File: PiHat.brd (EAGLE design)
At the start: 53.7 x 27.8 mm, 13 parts, among them J1 DESTINYSENSORFINAL_SPARKFUN-C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, X2 SCREENBREAKOUT_SCREENBREAKOUT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

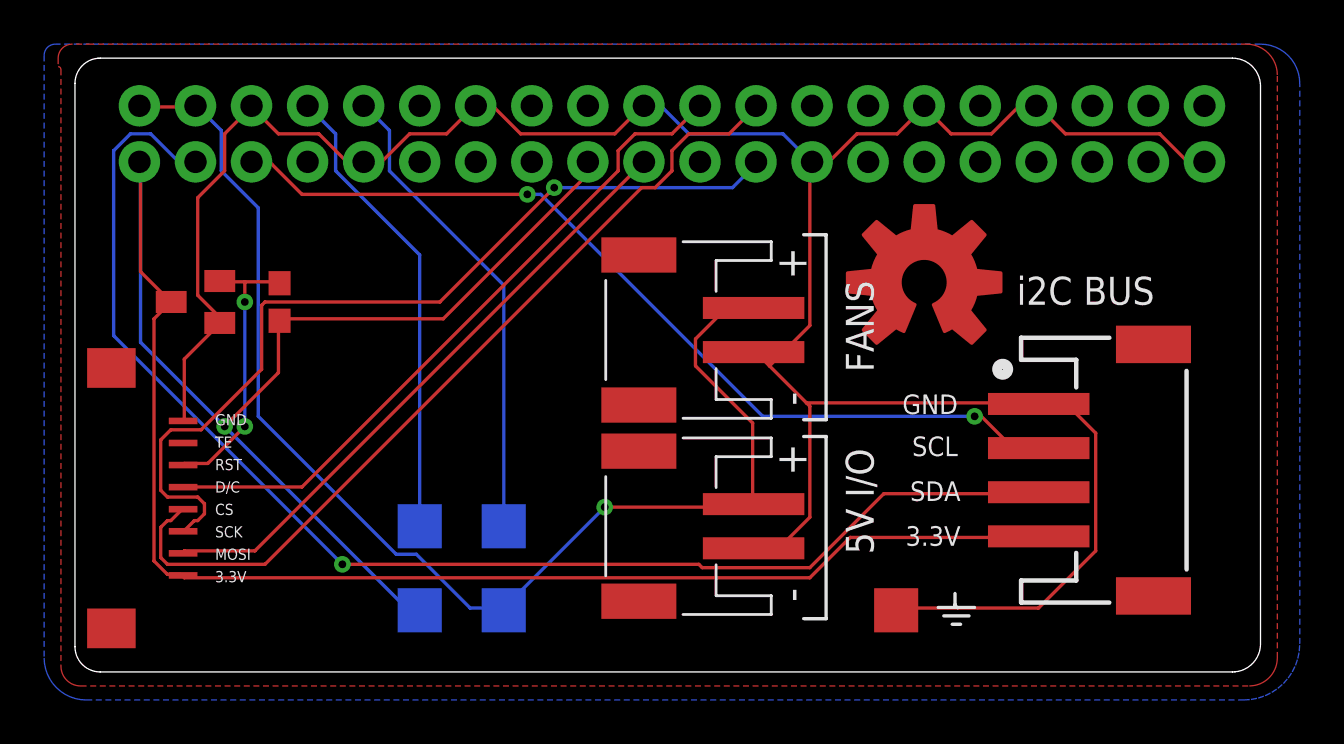
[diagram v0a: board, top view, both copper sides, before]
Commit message: pi HAT with preipherals for the office project need
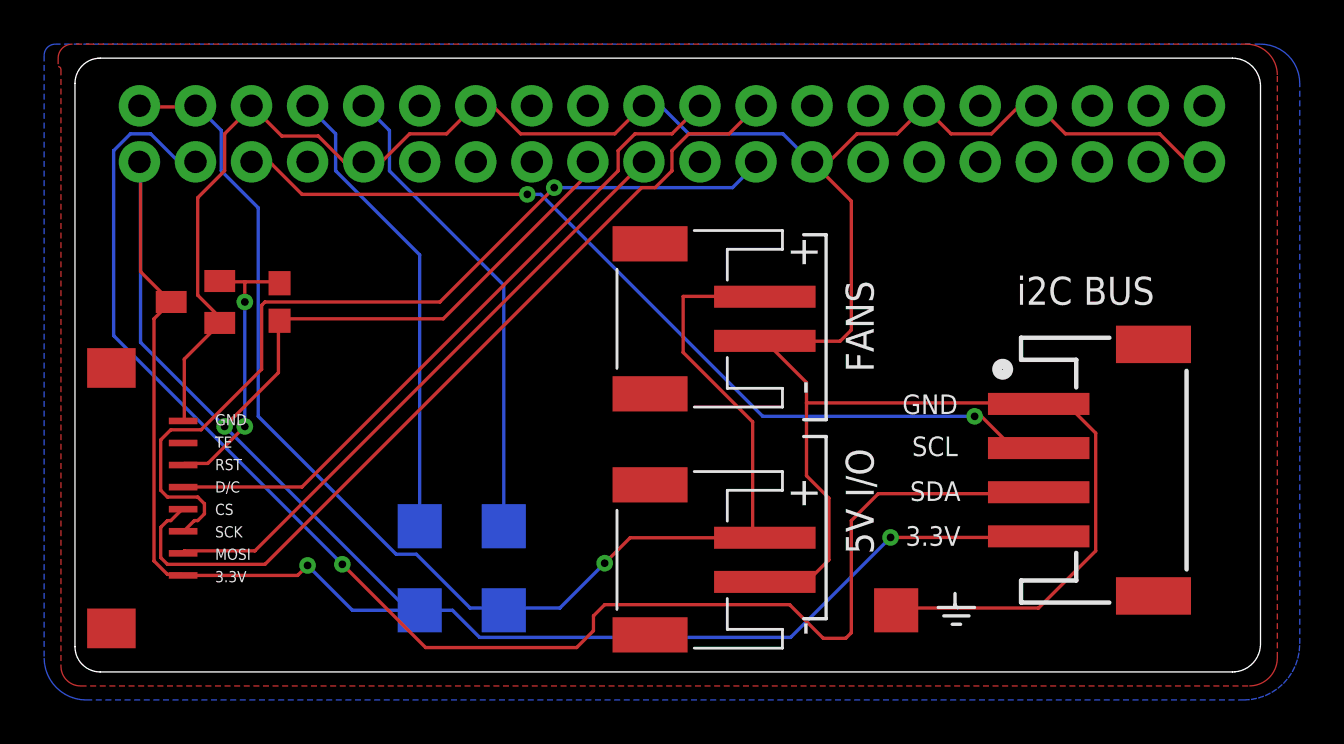
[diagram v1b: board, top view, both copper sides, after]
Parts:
- removed U$1: (no value), SparkFun-Aesthetics:OSHW-LOGO-L_COPPER
- moved 5V_IO 1.61 mm to (27.2, 3.56)
- moved FAN 0.72 mm to (27.2, 14.5)
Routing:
- net SDA: track 60.7 -> 68.3 mm
- net GND: track 117.2 -> 122.8 mm
- net 5V: track 57.8 -> 62.2 mm
- net 3.3V: track 109.2 -> 111.8 mm, vias 1 -> 3
